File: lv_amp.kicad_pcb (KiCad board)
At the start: 2 copper layers, 127 x 76.2 mm, 89 parts, among them J1 Jack-DC, J2 AudioJack2, J3 AudioJack2, Q1 Q_NMOS_DGS, U1 MAX1771xSA, U2 TL072, U3 ECC83, U4 ECC83, U5 ECC83

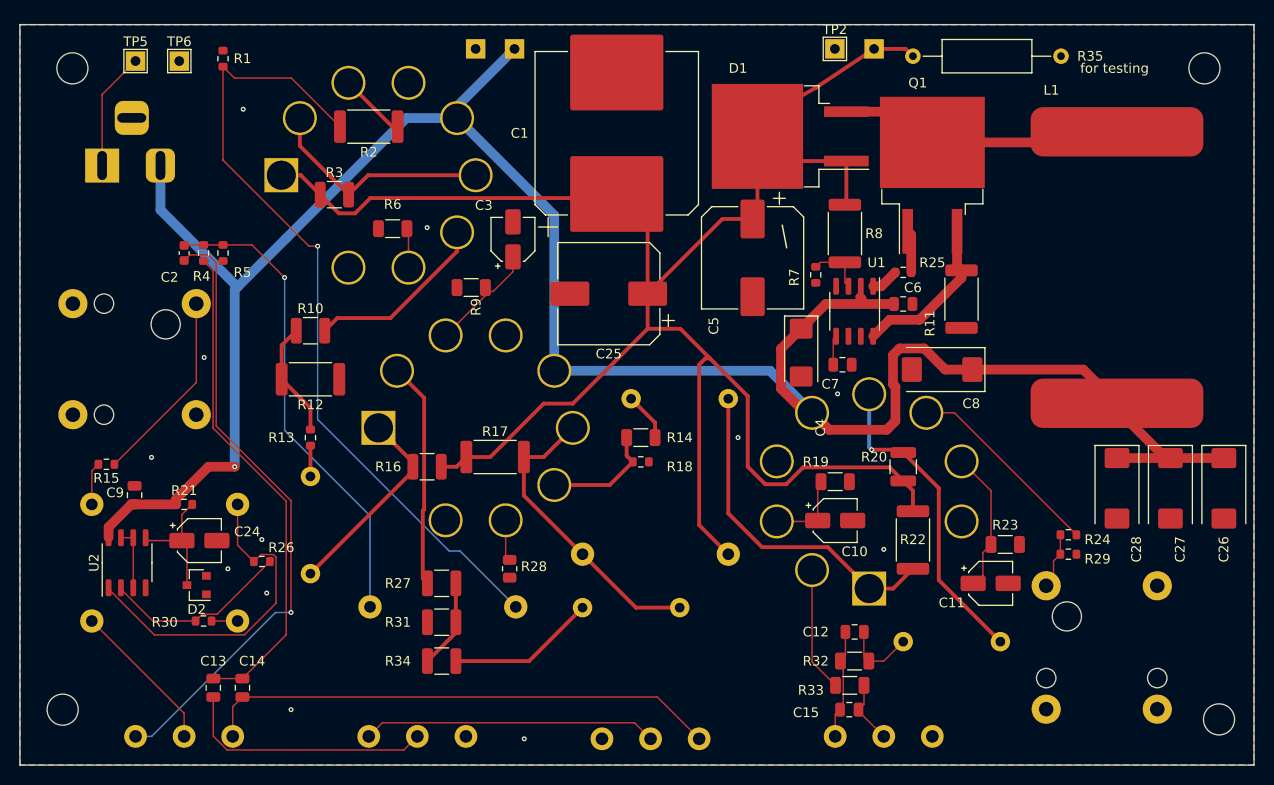
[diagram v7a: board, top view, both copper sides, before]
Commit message: power switch on hot side; fix drc fails in new version
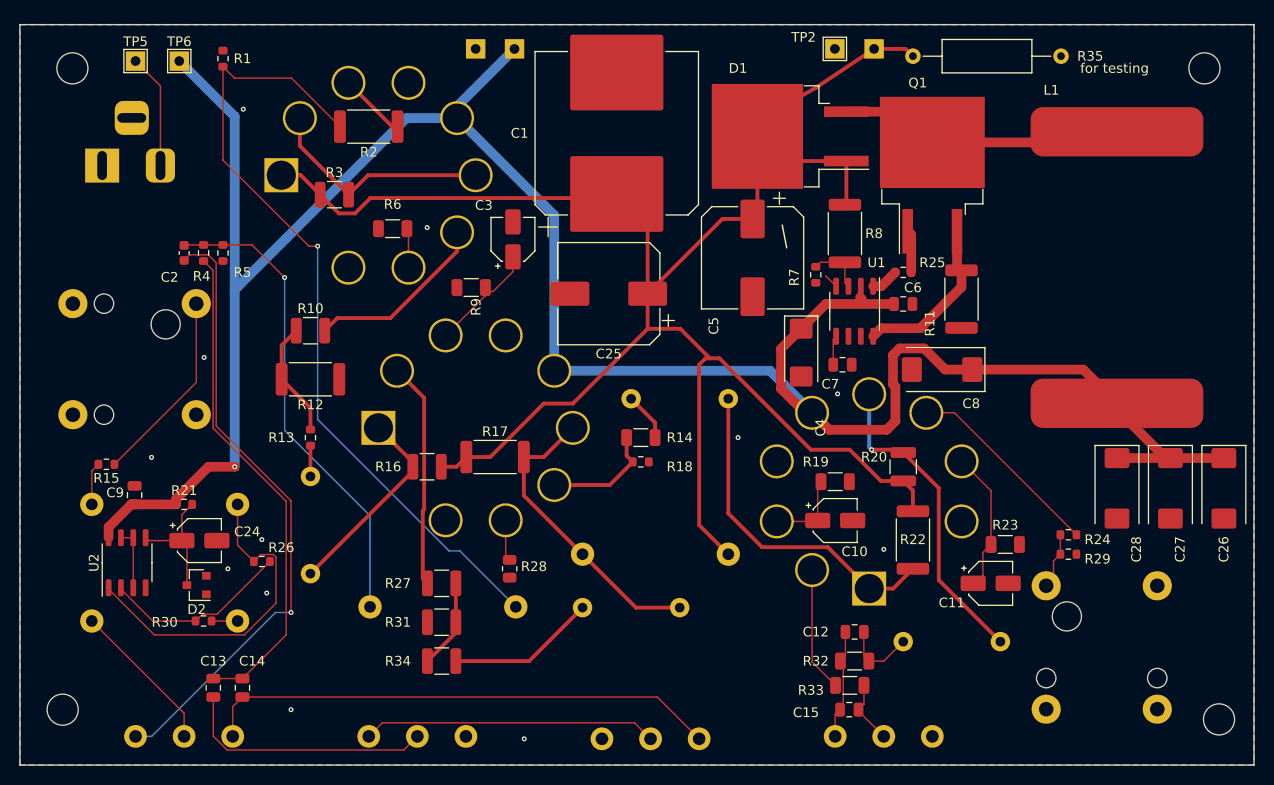
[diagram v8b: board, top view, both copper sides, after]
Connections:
- J1 pad 1: +12V -> Net-(J1-Pad1)
- J1 pad 2: Net-(J1-Pad2) -> GND
- TP5 pad 1: Net-(J1-Pad2) -> Net-(J1-Pad1)
- TP6 pad 1: GND -> +12V
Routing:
- net Net-(J1-Pad2): track 12.2 -> 0.00 mm
- net Net-(J1-Pad1): track 0.00 -> 11.8 mm
- net +12V: track 232.8 -> 242.9 mm
- net HT: track 200.3 -> 194.6 mm
- net GND: track 0.00 -> 1.55 mm
- net /q1s: track 16.6 -> 17.1 mm
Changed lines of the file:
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@@
 	(net 34 "unconnected-(J2-PadTN)")
 	(net 35 "Net-(D2-K)")
-	(net 36 "Net-(J1-Pad2)")
+	(net 36 "Net-(J1-Pad1)")
 	(net 37 "Net-(U3A-K)")
 	(net 38 "/u3ag")
@@
 		(tags "test point THT pad rectangle square")
 		(property "Reference" "TP2"
-			(at 0 -1.998 0)
+			(at -3.22 -1.2 0)
 			(layer "F.SilkS")
 			(effects
@@
 		)
 		(fp_text user "${REFERENCE}"
-			(at 0 -2 0)
+			(at -3.22 -1.25 0)
 			(layer "F.Fab")
 			(effects
@@
 			(layers "*.Cu" "*.Mask")
 			(remove_unused_layers no)
-			(net 9 "GND")
+			(net 17 "+12V")
 			(pinfunction "1")
 			(pintype "passive")
@@
 			(layers "*.Cu" "*.Mask")
 			(remove_unused_layers no)
-			(net 36 "Net-(J1-Pad2)")
+			(net 36 "Net-(J1-Pad1)")
 			(pinfunction "1")
 			(pintype "passive")
@@
 			(remove_unused_layers no)
 			(roundrect_rratio 0.25)
-			(net 17 "+12V")
+			(net 36 "Net-(J1-Pad1)")
 			(pintype "passive")
 		)
@@
 			(layers "*.Cu" "*.Mask")
 			(remove_unused_layers no)
-			(net 36 "Net-(J1-Pad2)")
+			(net 9 "GND")
 			(pintype "passive")
 		)
@@
 		(net 8)
 	)
+	(segment
+		(start 122.095 90.425)
+		(end 121 89.33)
+		(width 0.1524)
+		(layer "F.Cu")
+		(net 9)
+	)
 	(via
 		(at 51.64 108.04)
@@
 	)
 	(via
-		(at 61.08 72.21)
+		(at 61.083228 72.207285)
 		(size 0.508)
 		(drill 0.254)
@@
 	)
 	(segment
-		(start 60.2 90.8)
-		(end 60.2 109)
+		(start 60.2 72.95)
+		(end 60.2 90.8)
 		(width 1)
 		(layer "B.Cu")
@@
 	)
 	(segment
-		(start 52.56 78)
-		(end 52.56 82.56)
+		(start 54.5 67.25)
+		(end 60.2 72.95)
 		(width 1)
 		(layer "B.Cu")
@@
 	)
 	(segment
-		(start 93.090169 99.122148)
-		(end 115.296965 99.122148)
+		(start 60.2 90.8)
+		(end 60.2 109)
 		(width 1)
 		(layer "B.Cu")
@@
 	)
 	(segment
-		(start 52.56 82.56)
-		(end 60.5 90.5)
+		(start 93.090169 99.122148)
+		(end 115.296965 99.122148)
 		(width 1)
 		(layer "B.Cu")
@@
 	)
 	(segment
-		(start 127.60048 109.06298)
-		(end 118.696497 109.06298)
-		(width 0.4)
-		(layer "F.Cu")
-		(net 21)
-	)
-	(segment
 		(start 116.54 77.54)
 		(end 114 75)
@@
 	)
 	(segment
-		(start 118.696497 109.06298)
-		(end 116.959957 110.79952)
-		(width 0.4)
-		(layer "F.Cu")
-		(net 21)
-	)
-	(segment
 		(start 72.589382 82.92452)
 		(end 70.92452 82.92452)
@@
 	)
 	(segment
-		(start 116.959957 110.79952)
-		(end 114.79952 110.79952)
-		(width 0.4)
-		(layer "F.Cu")
-		(net 21)
-	)
-	(segment
 		(start 102.7 91.19)
 		(end 102.7 84.11)
@@
 	)
 	(segment
-		(start 114.79952 110.79952)
-		(end 113 109)
+		(start 114 83)
+		(end 114 75)
 		(width 0.4)
 		(layer "F.Cu")
@@
 	)
 	(segment
-		(start 114 83)
-		(end 114 75)
+		(start 110.093974 97.843974)
+		(end 109.106026 97.843974)
 		(width 0.4)
 		(layer "F.Cu")
@@
 	)
 	(segment
+		(start 126.7125 110.4625)
+		(end 123.5 107.25)
+		(width 0.4)
+		(layer "F.Cu")
+		(net 21)
+	)
+	(segment
 		(start 95 102.5)
 		(end 102.7 94.8)
@@
 	)
 	(segment
-		(start 113 101.737949)
-		(end 113 109)
-		(width 0.4)
-		(layer "F.Cu")
-		(net 21)
-	)
-	(segment
 		(start 67 79)
 		(end 65 79)
@@
 	)
 	(segment
-		(start 109.106026 97.843974)
-		(end 113 101.737949)
+		(start 119.5 107.25)
+		(end 110.093974 97.843974)
 		(width 0.4)
 		(layer "F.Cu")
@@
 	)
 	(segment
+		(start 129 110.4625)
+		(end 126.7125 110.4625)
+		(width 0.4)
+		(layer "F.Cu")
+		(net 21)
+	)
+	(segment
 		(start 102.7 94.8)
 		(end 102.7 91.19)
@@
 	)
 	(segment
-		(start 111 118)
-		(end 108 115)
+		(start 123.5 107.25)
+		(end 119.5 107.25)
 		(width 0.4)
 		(layer "F.Cu")
@@
 	)
 	(segment
-		(start 129 110.4625)
-		(end 127.60048 109.06298)
+		(start 111 118)
+		(end 108 115)
 		(width 0.4)
 		(layer "F.Cu")
@@
 	)
 	(segment
-		(start 130.676146 93.87452)
-		(end 135 89.550666)
+		(start 126.73 94.75)
+		(end 130.75 94.75)
 		(width 1)
 		(layer "F.Cu")
@@
 	)
 	(segment
-		(start 125.905 95.575)
-		(end 127.60548 93.87452)
+		(start 135 90.5)
+		(end 135 88.7875)
 		(width 1)
 		(layer "F.Cu")
@@
 	)
 	(segment
-		(start 127.60548 93.87452)
-		(end 130.676146 93.87452)
+		(start 134.54 88.3275)
+		(end 135 88.7875)
 		(width 1)
 		(layer "F.Cu")
@@
 	)
 	(segment
-		(start 135 89.550666)
-		(end 135 88.7875)
+		(start 125.905 95.575)
+		(end 126.73 94.75)
 		(width 1)
 		(layer "F.Cu")
@@
 	)
 	(segment
-		(start 134.54 88.3275)
-		(end 135 88.7875)
+		(start 130.75 94.75)
+		(end 135 90.5)
 		(width 1)
 		(layer "F.Cu")
@@
 	)
 	(segment
-		(start 46.56 78)
-		(end 46.56 70.69)
+		(start 52.56 69.81)
+		(end 52.56 78)
 		(width 0.1524)
 		(layer "F.Cu")
@@
 	)
 	(segment
-		(start 46.56 70.69)
-		(end 50 67.25)
+		(start 50 67.25)
+		(end 52.56 69.81)
 		(width 0.1524)
 		(layer "F.Cu")
